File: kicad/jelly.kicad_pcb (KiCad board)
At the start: 2 copper layers, 59.9 x 32.9 mm, 23 parts, among them M1 PAGER_MOTOR, M2 PAGER_MOTOR, P1 CONN_01X01, P10 CONN_01X01, P2 CONN_01X01, P3 CONN_01X01, P4 CONN_01X01, P5 CONN_01X01, P6 CONN_01X01, P7 CONN_01X01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

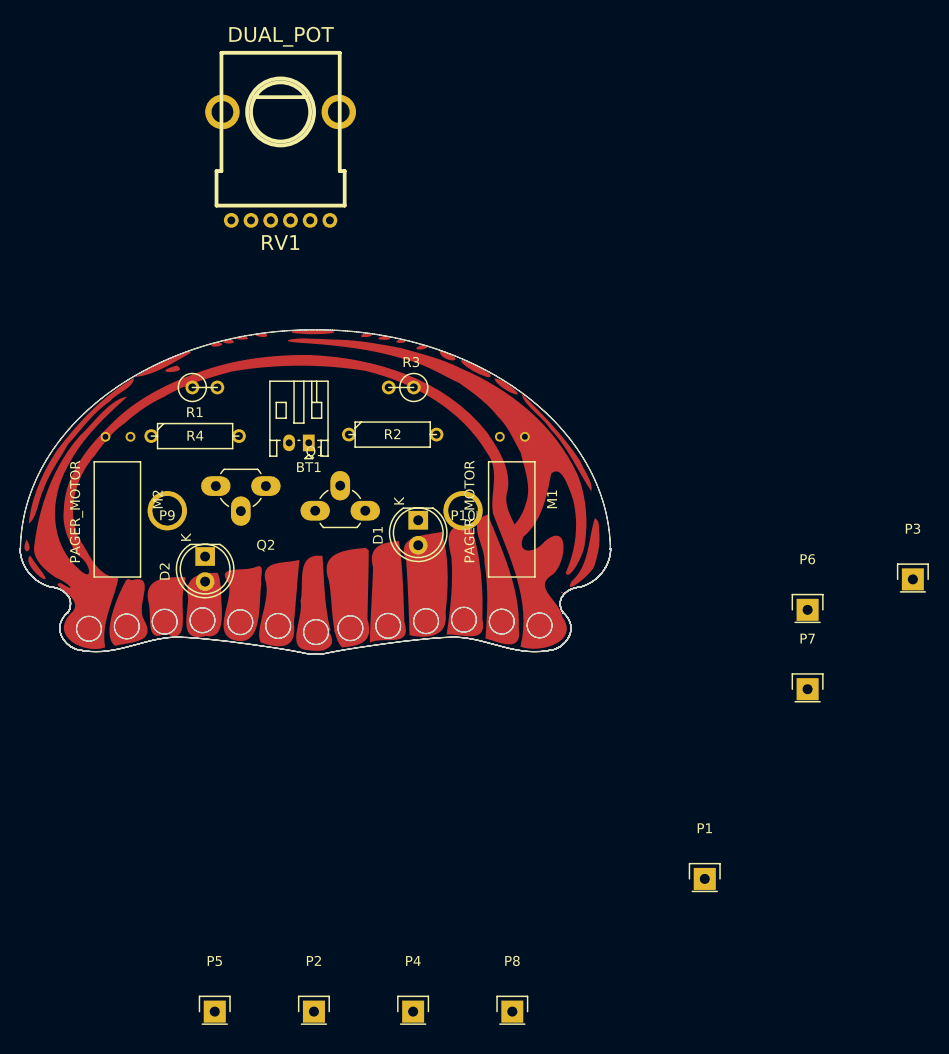
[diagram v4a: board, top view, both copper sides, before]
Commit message: Add LDR silkscreen image
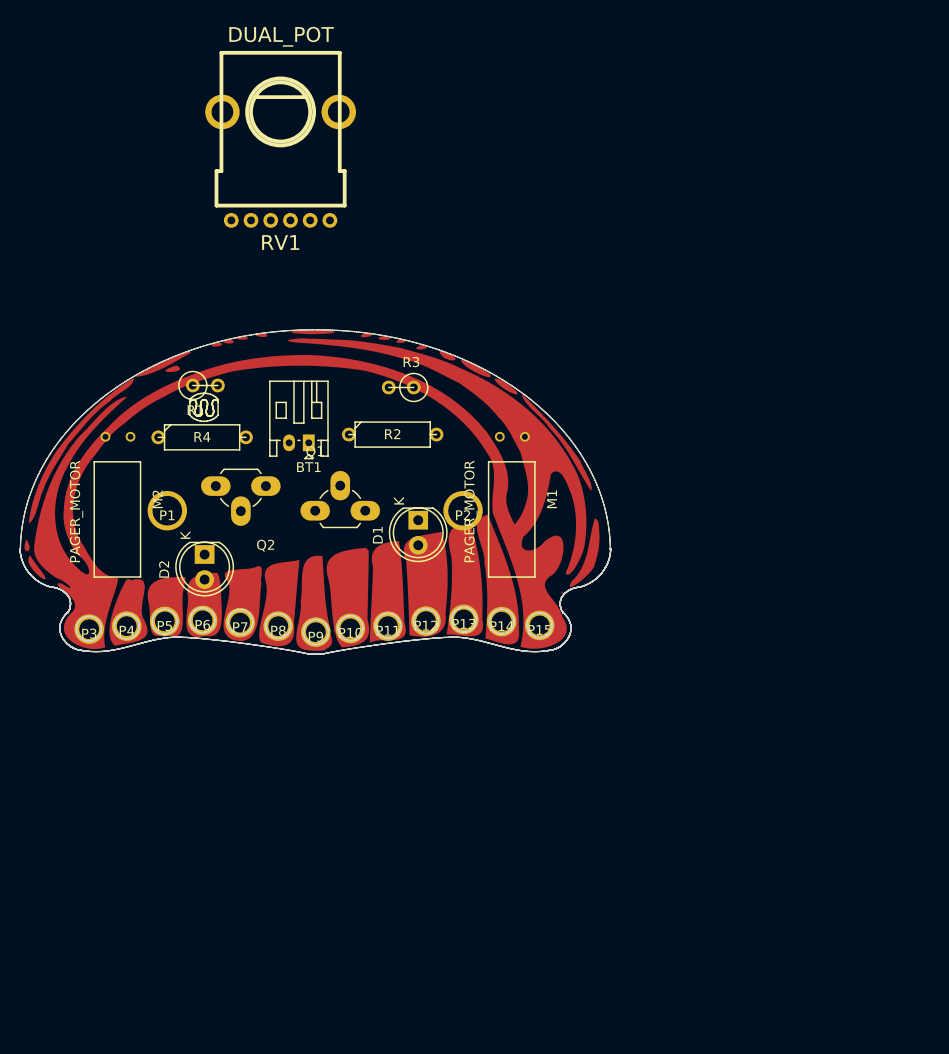
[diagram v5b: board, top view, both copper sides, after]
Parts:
- added P11: CONN_01X01, custom:hole2, F.Cu at (157.4, 94.2)
- added P12: CONN_01X01, custom:hole2, F.Cu at (161.2, 93.7)
- added P13: CONN_01X01, custom:hole2, F.Cu at (165.1, 93.5)
- added P14: CONN_01X01, custom:hole2, F.Cu at (168.9, 93.8)
- added P15: CONN_01X01, custom:hole2, F.Cu at (172.8, 94.1)
- added svg2mod: G***, custom:ldr, F.Cu at (138.7, 72.0)
- DNP1: footprint footprints:jelly -> custom:jelly
- M1, M2: footprint footprints:pager_motor_custom -> custom:pager_motor_custom
- P1, P2: footprint KiCad/Pin_Headers.pretty:Pin_Header_Straight_1x01 -> custom:hole
- P10, P9: footprint footprints:hole -> custom:hole2
- P3, P4, P5, P6, P7, P8: footprint KiCad/Pin_Headers.pretty:Pin_Header_Straight_1x01 -> custom:hole2
- moved P3 83.7 mm to (127.1, 94.5)
- moved P1 66.1 mm to (135.0, 82.5)
- moved P6 61.4 mm to (138.6, 93.6)
- moved P7 57.9 mm to (142.4, 93.9)
- moved P2 53.0 mm to (165.0, 82.5)
- moved P4 48.7 mm to (130.9, 94.2)
- moved P8 45.7 mm to (146.3, 94.2)
- moved P5 39.9 mm to (134.7, 93.7)
- moved P9 19.5 mm to (150.1, 94.8)
- moved P10 16.5 mm to (153.6, 94.4)
- moved R4 0.72 mm to (138.5, 75.1)
- moved D2 0.21 mm to (138.8, 86.9)
- moved R1 0.21 mm to (138.9, 69.8)
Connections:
- D1 pad 1: VCC -> Net-(D1-Pad1)
- D1 pad 2: Net-(D1-Pad2) -> Vout1
- D2 pad 1: VCC -> Net-(D2-Pad1)
- D2 pad 2: Net-(D2-Pad2) -> Vout2
- P1 pad 1: VCC -> Net-(P1-Pad1)
- P10 pad 1: Net-(P10-Pad1) -> Vout2
- P2 pad 1: VCC -> Net-(P2-Pad1)
- P3 pad 1: Vout1 -> VCC
- P4 pad 1: Vout2 -> VCC
- P7 pad 1: VCC -> Vout1
- P8 pad 1: VCC -> Vout2
- P9 pad 1: Net-(P9-Pad1) -> Vout1
- R2 pad 1: Vout1 -> Net-(D1-Pad1)
- R2 pad 2: Net-(D1-Pad2) -> VCC
- R4 pad 1: Vout2 -> Net-(D2-Pad1)
- R4 pad 2: Net-(D2-Pad2) -> VCC

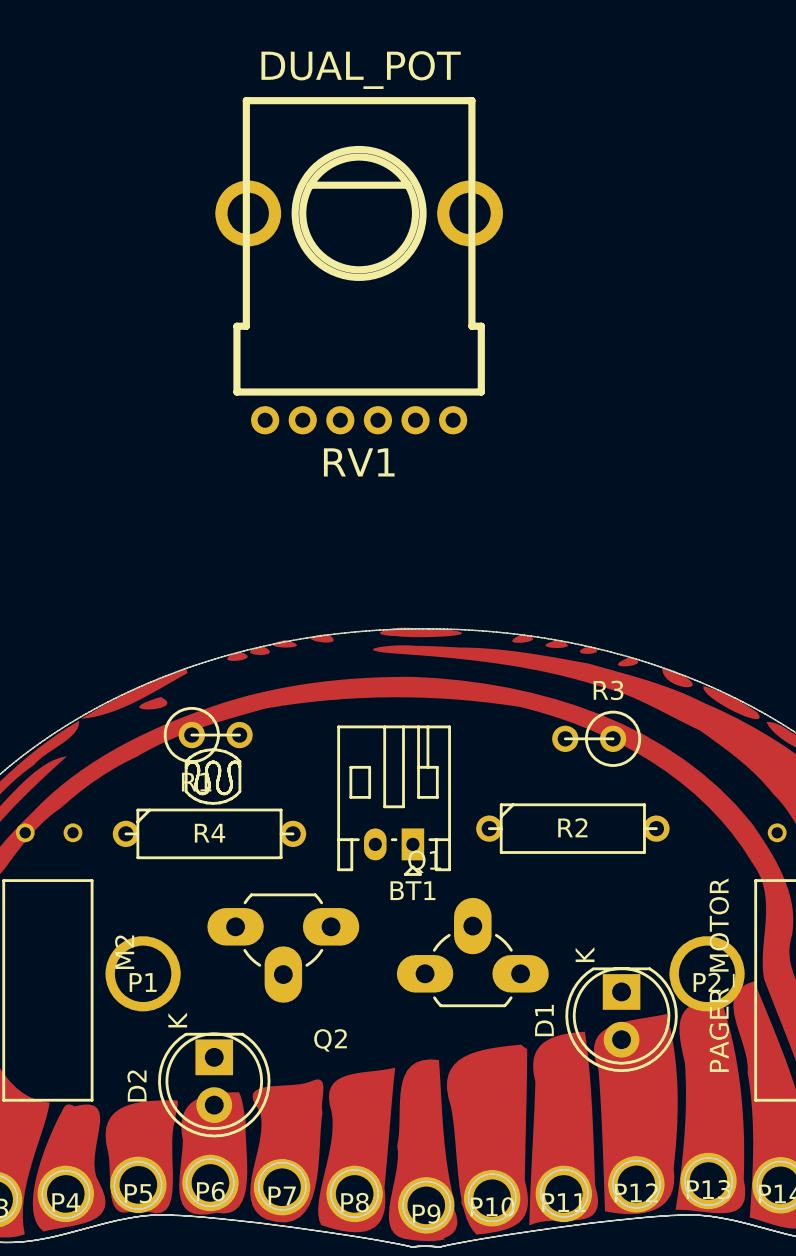
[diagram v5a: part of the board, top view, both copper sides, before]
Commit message: Re-arrange connector holes
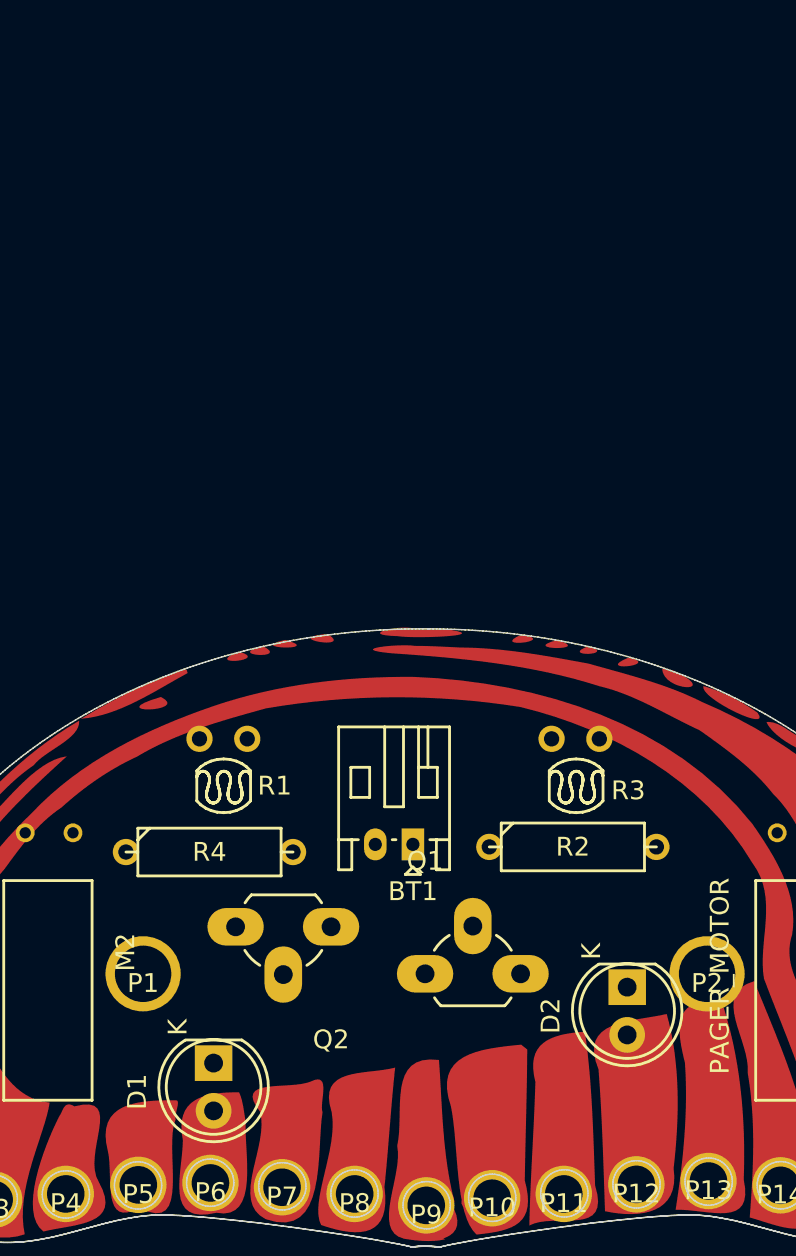
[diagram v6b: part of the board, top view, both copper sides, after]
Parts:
- removed RV1: DUAL_POT, pelrun/libKiCad/footprint/w_pth_resistors.pretty:trimmer_alps_rk12l12c0-f20-c0
- removed svg2mod: G***, custom:ldr
- added DNP2: ldr_image, custom:ldr_image, F.Cu at (139.2, 72.5)
- added DNP3: ldr_image, custom:ldr_image, F.Cu at (158.0, 72.5)
- R1, R3: value 220 -> Photores; footprint KiCad/Discret.pretty:R1 -> custom:ldr
- R2: value R -> 220
- moved D2 22.3 mm to (160.8, 83.2)
- moved D1 22.0 mm to (138.8, 87.2)
- moved R2 0.97 mm to (157.9, 75.8)
- moved R4 0.97 mm to (138.5, 76.0)
- moved R3 0.73 mm to (158.0, 70.0), turned to 0 degrees
- moved R1 0.45 mm to (139.3, 70.0), turned to 180 degrees
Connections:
- P10 pad 1: Vout2 -> GND
- P12 pad 1: Vout2 -> Vout1
- P13 pad 1: VCC -> Vout1
- P6 pad 1: Vout2 -> Vout1
- P8 pad 1: Vout2 -> GND
- P9 pad 1: Vout1 -> GND
- R1 pad 1: VCC -> Net-(Q1-Pad2)
- R1 pad 2: Net-(Q1-Pad2) -> VCC
- R3 pad 1: VCC -> Net-(Q2-Pad2)
- R3 pad 2: Net-(Q2-Pad2) -> VCC

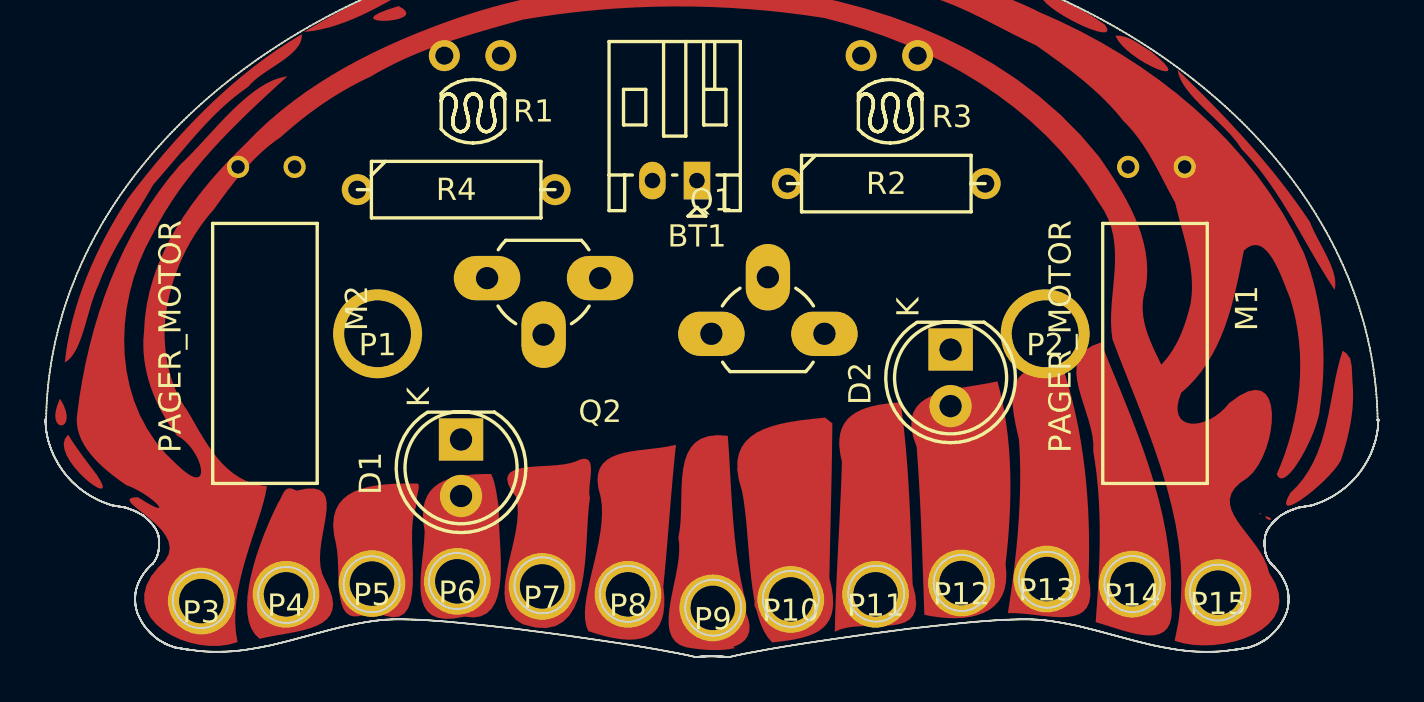
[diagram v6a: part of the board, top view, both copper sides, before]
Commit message: Add notches to outline and remove holes
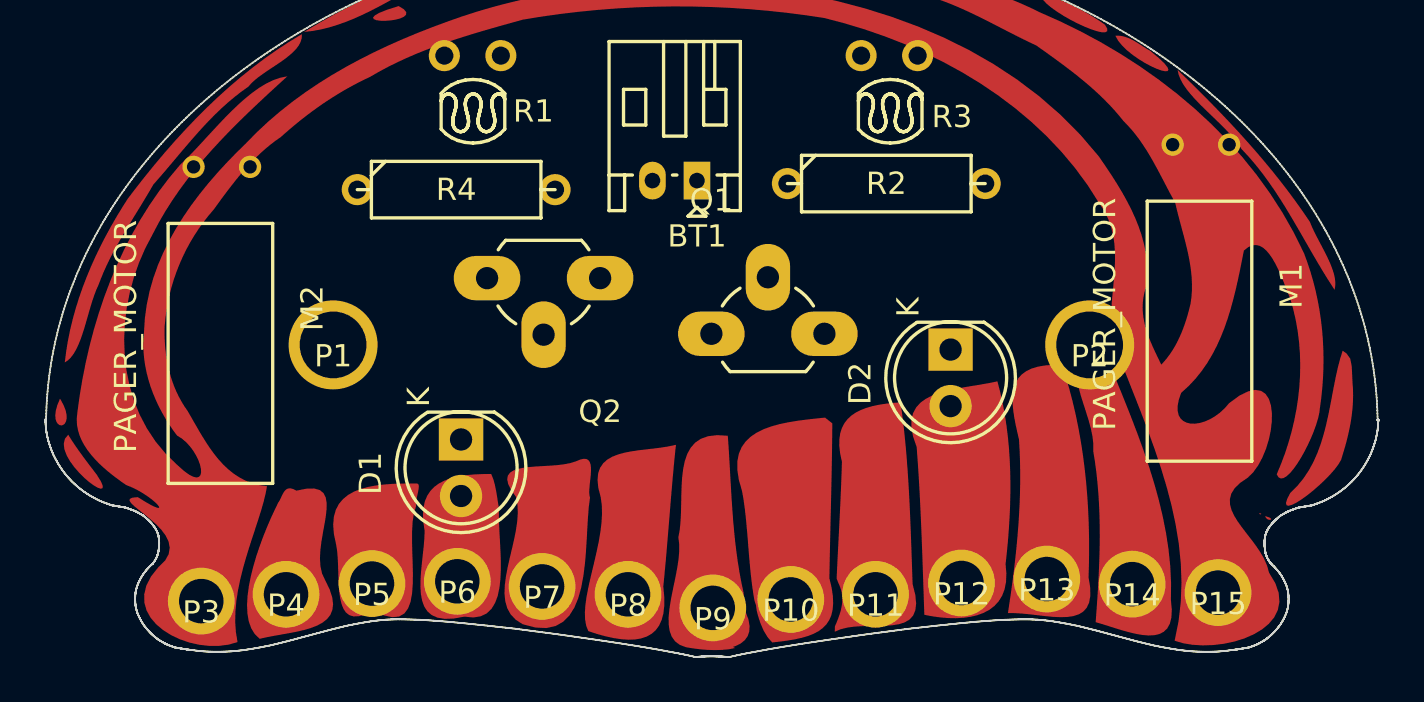
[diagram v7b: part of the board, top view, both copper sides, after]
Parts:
- moved M1 2.24 mm to (172.0, 74.0)
- moved P1 2.06 mm to (133.0, 83.0)
- moved P2 2.06 mm to (167.0, 83.0)
- moved M2 2.00 mm to (128.0, 75.0)
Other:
- outline, holes or cut-outs redrawn

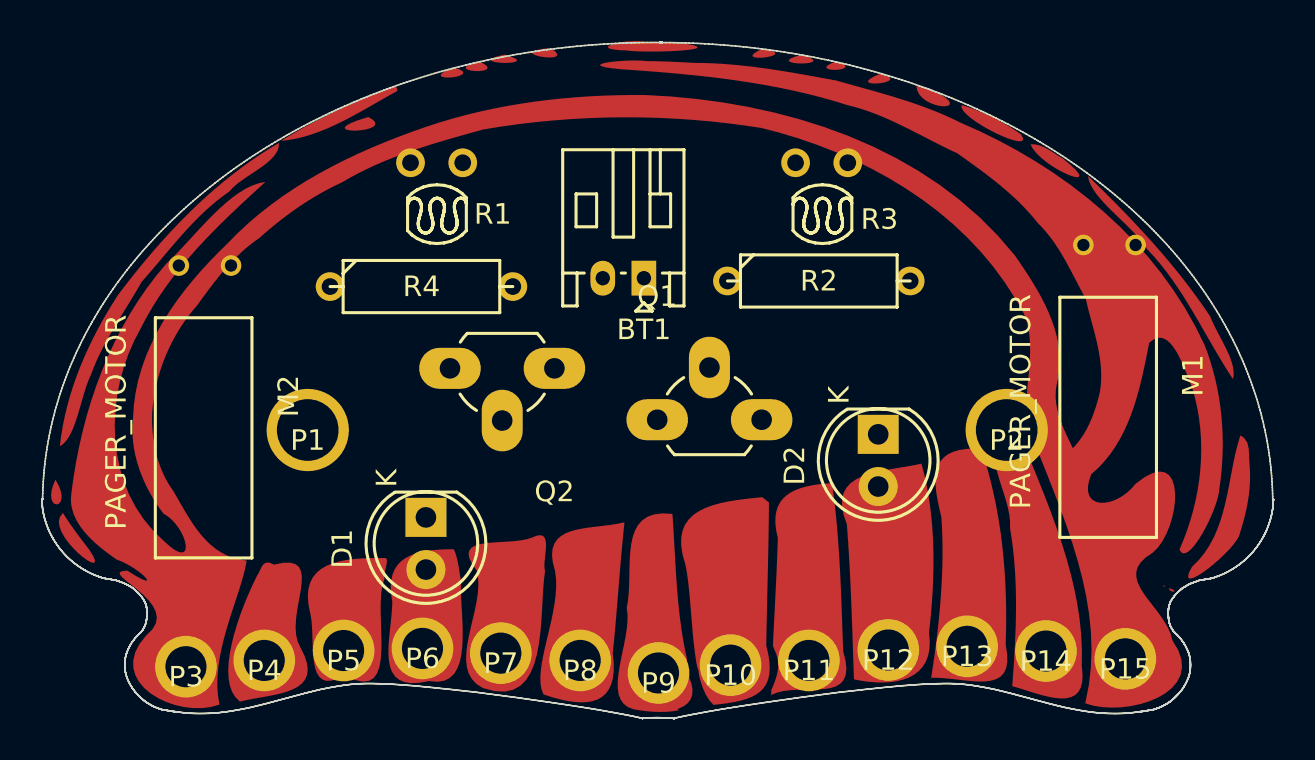
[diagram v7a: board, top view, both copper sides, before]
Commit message: Adjust copper specks near edges
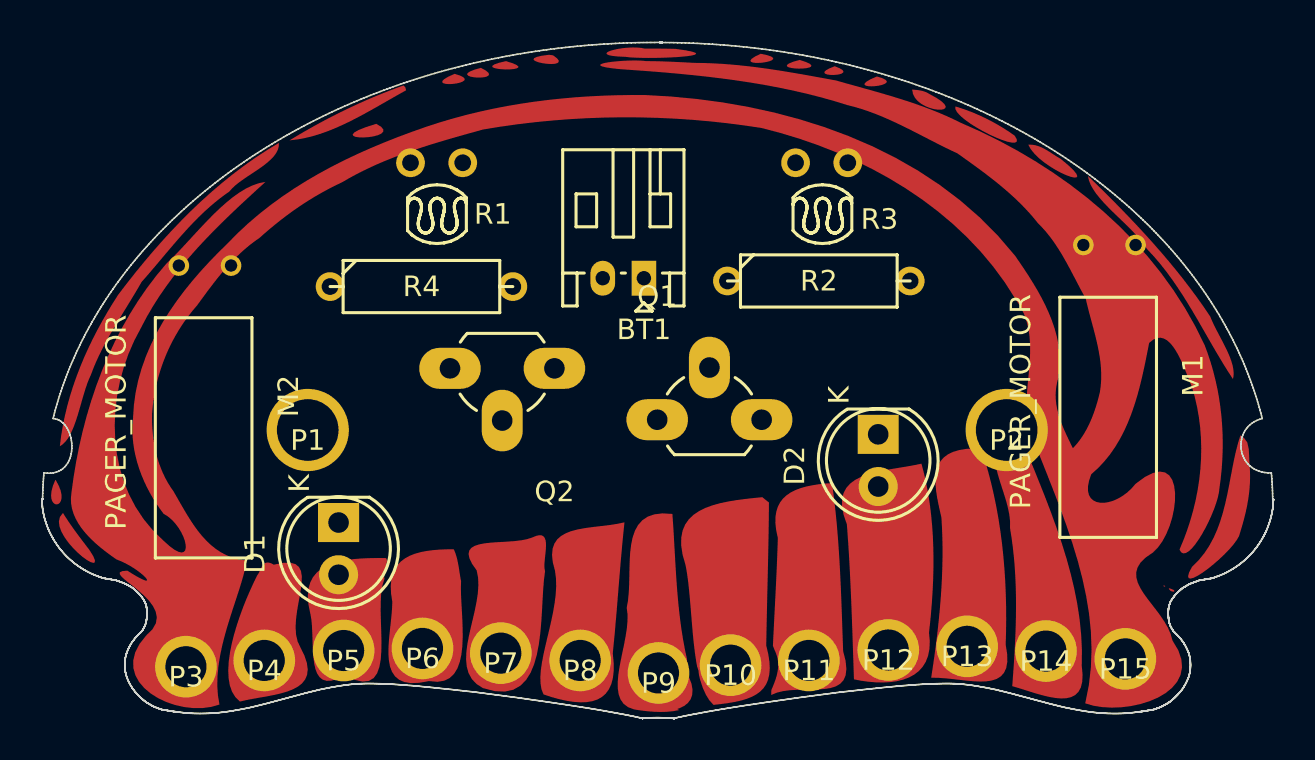
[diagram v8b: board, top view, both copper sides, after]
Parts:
- moved D1 4.26 mm to (134.5, 87.5)
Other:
- outline, holes or cut-outs redrawn
